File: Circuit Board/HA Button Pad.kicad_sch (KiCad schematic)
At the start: 59 parts, among them J1 Barrel_Jack, P1 USB C Connector, Q1 PN2222A, SW1 Button 1, SW2 Button 2, SW3 Button 3, SW4 Button 4, SW5 Bank Up, SW6 Bank Down, SW7 Program Button, U1 WT32-ETH01, U3 CP2102N, U4 Char LCD I2C, U5 Button I2C

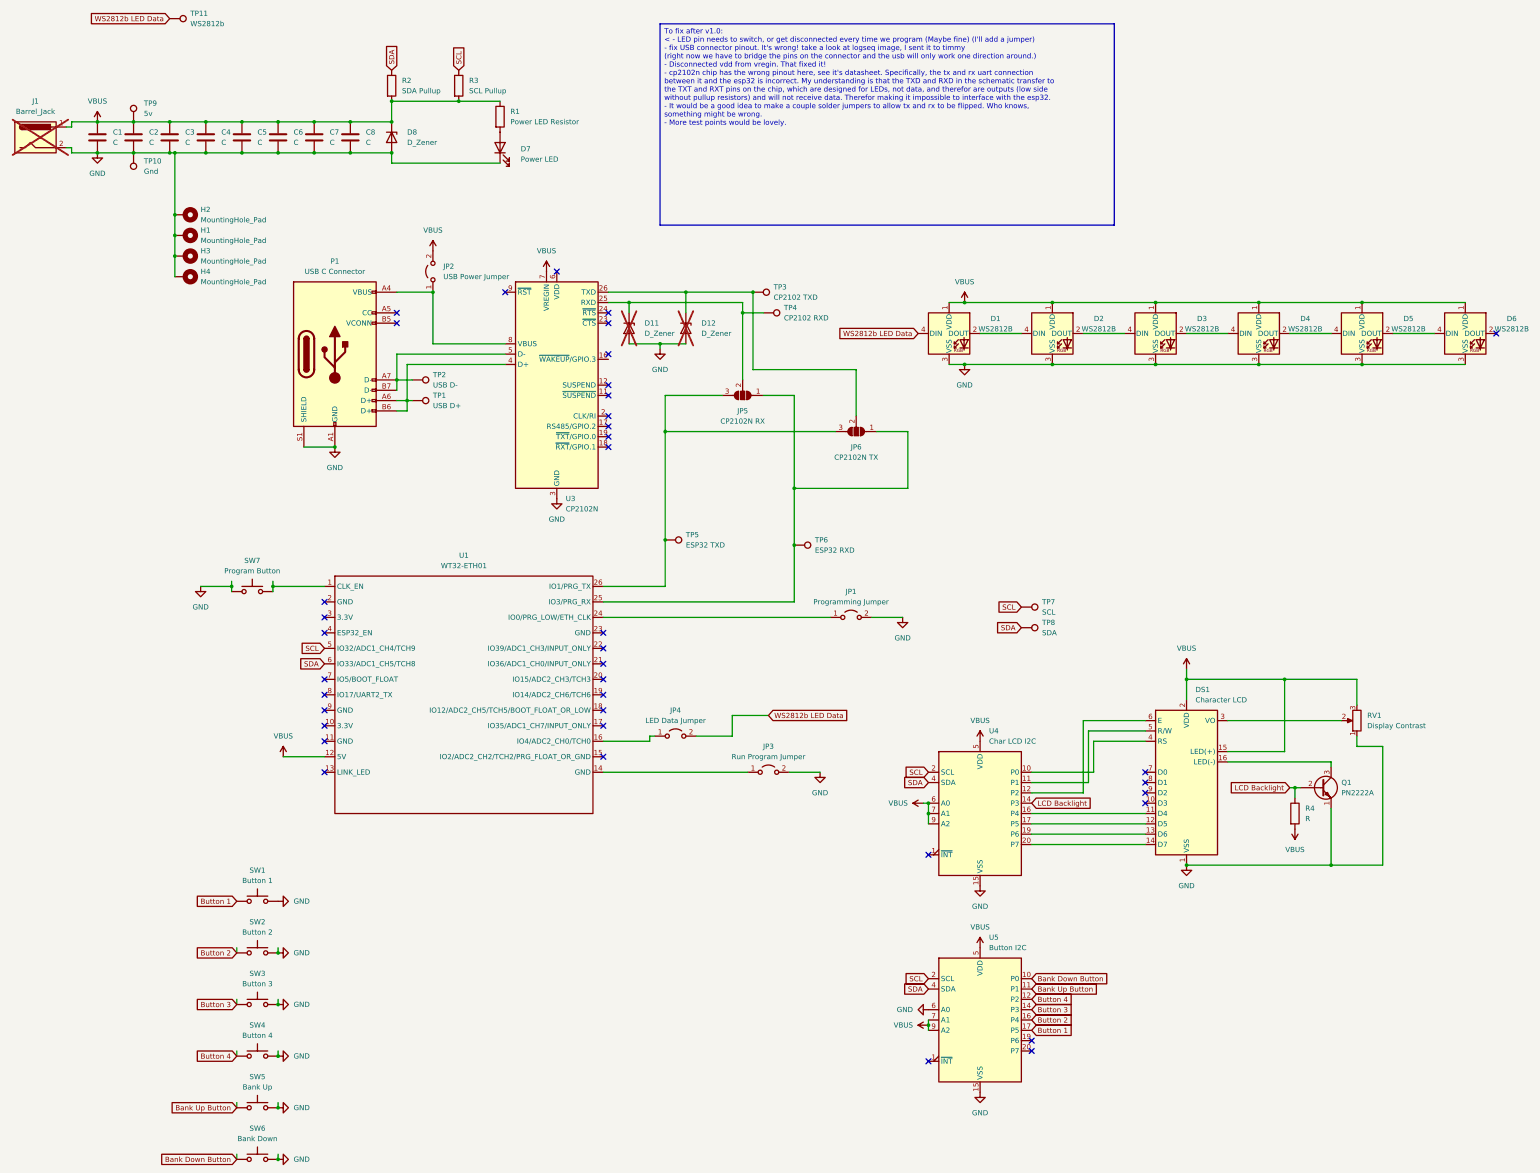
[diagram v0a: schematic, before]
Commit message: Added Capacitive Touch, changed ESP32 Pin Assignment
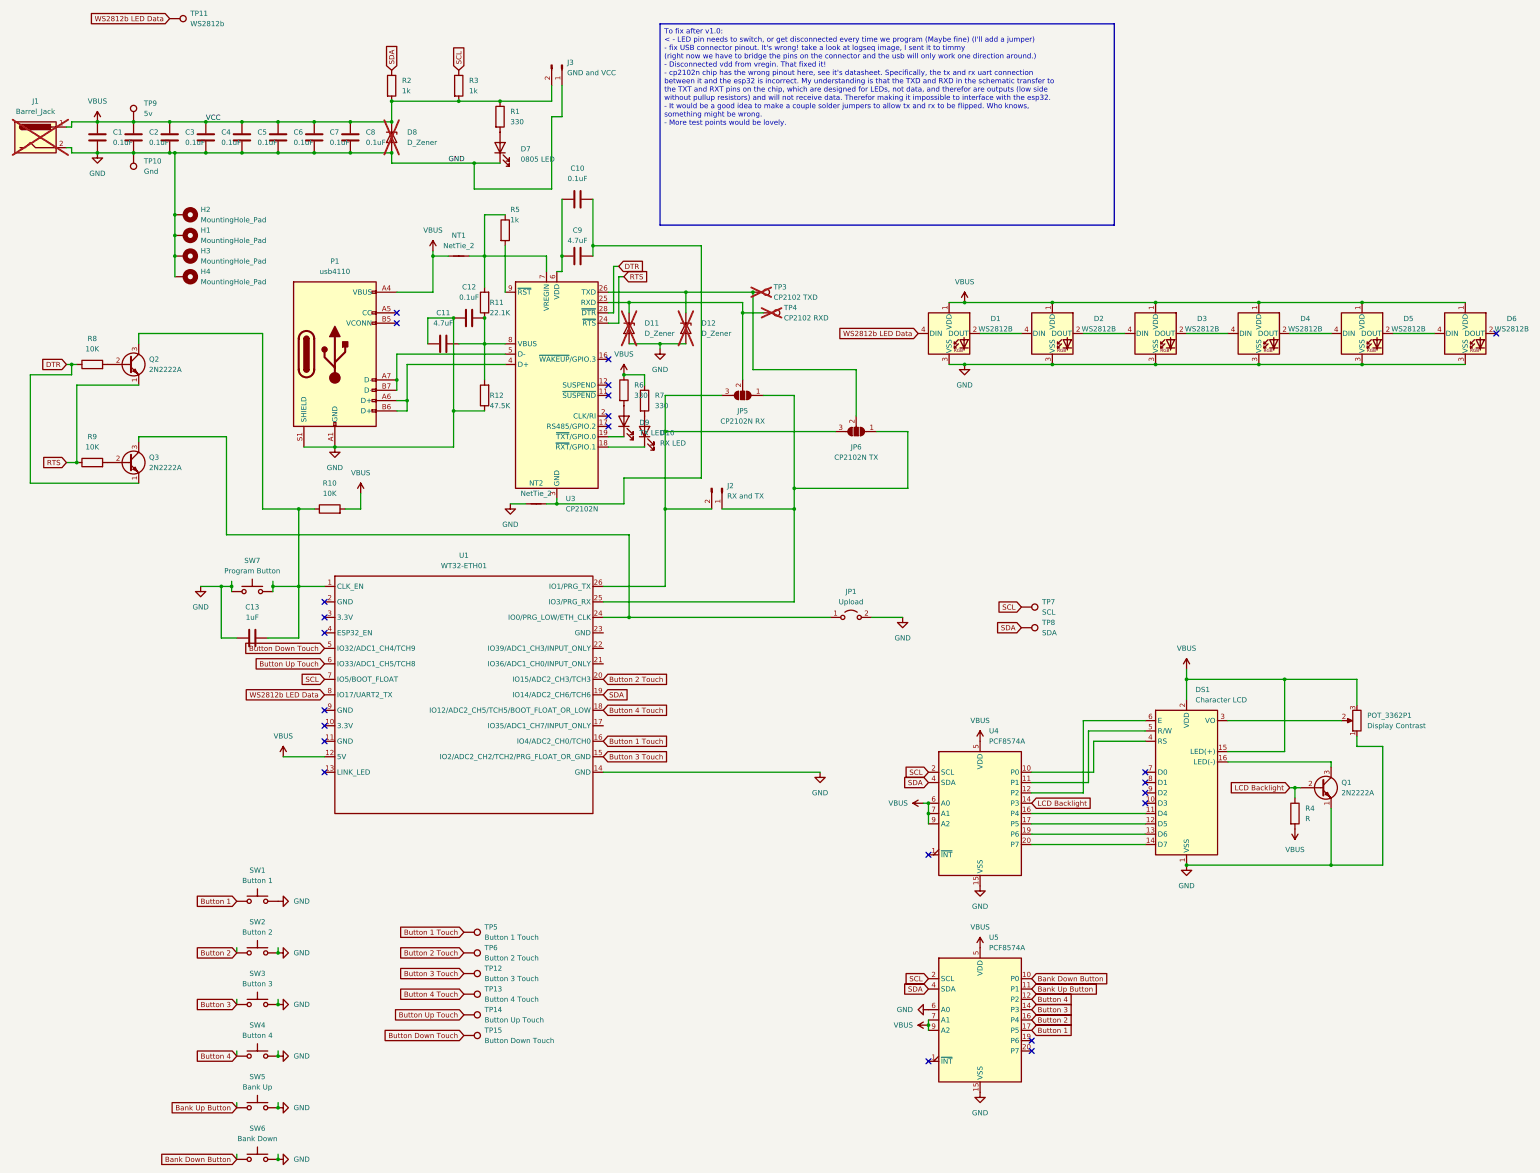
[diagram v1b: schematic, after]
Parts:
- removed JP2: USB Power Jumper, Connector_PinHeader_2.54mm:PinHeader_1x02_P2.54mm_Vertical, symbol Jumper:Jumper_2_Open
- removed JP3: Run Program Jumper, Connector_PinHeader_2.54mm:PinHeader_1x02_P2.54mm_Vertical, symbol Jumper:Jumper_2_Open
- removed JP4: LED Data Jumper, Connector_PinHeader_2.54mm:PinHeader_1x02_P2.54mm_Vertical, symbol Jumper:Jumper_2_Open
- removed TP1: USB D+, TestPoint:TestPoint_Pad_D1.0mm, symbol Connector:TestPoint
- removed TP2: USB D-, TestPoint:TestPoint_Pad_D1.0mm, symbol Connector:TestPoint
- added C10, C12: 0.1uF, capacitor model:CAPC340180_88N_KEM, symbol Device:C
- added C11, C9: 4.7uF, capacitor model:CAPC340180_88N_KEM, symbol Device:C
- added C13: 1uF, capacitor model:CAPC340180_88N_KEM, symbol Device:C
- added D10: RX LED, LED_SMD:LED_0805_2012Metric, symbol Device:LED
- added D9: TX LED, LED_SMD:LED_0805_2012Metric, symbol Device:LED
- added J2: RX and TX, Connector_PinHeader_2.54mm:PinHeader_1x02_P2.54mm_Vertical, symbol Connector:Conn_01x02_Pin
- added J3: GND and VCC, Connector_PinHeader_2.54mm:PinHeader_1x02_P2.54mm_Vertical, symbol Connector:Conn_01x02_Pin
- added NT1, NT2: NetTie_2, NetTie:NetTie-2_SMD_Pad0.5mm, symbol Device:NetTie_2
- added Q2, Q3: 2N2222A, Package_TO_SOT_THT:TO-92_Inline, symbol Transistor_BJT:PN2222A
- added R10, R8, R9: 10K, Resistor_SMD:R_0805_2012Metric, symbol Device:R
- added R11: 22.1K, Resistor_SMD:R_0805_2012Metric, symbol Device:R
- added R12: 47.5K, Resistor_SMD:R_0805_2012Metric, symbol Device:R
- added R5: 1k, Resistor_SMD:R_0805_2012Metric, symbol Device:R
- added R6, R7: 330, Resistor_SMD:R_0805_2012Metric, symbol Device:R
- added TP12: Button 3 Touch, TestPoint:TestPoint_THTPad_2.5x2.5mm_Drill1.2mm, symbol Connector:TestPoint
- added TP13: Button 4 Touch, TestPoint:TestPoint_THTPad_2.5x2.5mm_Drill1.2mm, symbol Connector:TestPoint
- added TP14: Button Up Touch, TestPoint:TestPoint_THTPad_2.5x2.5mm_Drill1.2mm, symbol Connector:TestPoint
- added TP15: Button Down Touch, TestPoint:TestPoint_THTPad_2.5x2.5mm_Drill1.2mm, symbol Connector:TestPoint
- C1, C2, C3, C4, C5, C6, C7, C8: value C -> 0.1uF
- D7: value Power LED -> 0805 LED; footprint LED_SMD:LED_0603_1608Metric -> LED_SMD:LED_0805_2012Metric
- D8, TP3, TP4: now not fitted; now left out of the parts list
- DS1, SW1, SW2, SW3, SW4, SW5, SW6, U1: now left out of the parts list
- JP1: value Programming Jumper -> Upload
- P1: value USB C Connector -> usb4110
- Q1: value PN2222A -> 2N2222A
- R1: value Power LED Resistor -> 330; footprint Resistor_SMD:R_0603_1608Metric -> Resistor_SMD:R_0805_2012Metric
- R2: value SDA Pullup -> 1k; footprint Resistor_SMD:R_0603_1608Metric -> Resistor_SMD:R_0805_2012Metric
- R3: value SCL Pullup -> 1k; footprint Resistor_SMD:R_0603_1608Metric -> Resistor_SMD:R_0805_2012Metric
- R4: footprint Resistor_SMD:R_0603_1608Metric -> Resistor_SMD:R_0805_2012Metric
- TP5: value ESP32 TXD -> Button 1 Touch; footprint TestPoint:TestPoint_Pad_D1.0mm -> TestPoint:TestPoint_THTPad_2.5x2.5mm_Drill1.2mm
- TP6: value ESP32 RXD -> Button 2 Touch; footprint TestPoint:TestPoint_Pad_D1.0mm -> TestPoint:TestPoint_THTPad_2.5x2.5mm_Drill1.2mm
- U4: value Char LCD I2C -> PCF8574A
- U5: value Button I2C -> PCF8574A
- renumbered RV1 to POT_3362P1
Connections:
- net GND: now also U1.14 (GND), C11.1, C12.1, C13.1, J3.1 (Pin_1), NT2.1, R12.1; no longer U3.12 (SUSPEND), U3.21 (GND), U3.3 (GND)
- net SCL: now also U1.7 (IO5/BOOT_FLOAT); no longer U1.5 (IO32/ADC1_CH4/TCH9)
- net SDA: now also U1.19 (IO14/ADC2_CH6/TCH6); no longer U1.6 (IO33/ADC1_CH5/TCH8)
- net VBUS: now also P1.A4 (VBUS), P1.A9 (VBUS), P1.B4 (VBUS), P1.B9 (VBUS), J3.2 (Pin_2), NT1.1, R10.2, R6.1, R7.1; no longer U3.7 (VREGIN)
- net WS2812b LED Data: now also U1.8 (IO17/UART2_TX)
- net at JP5.1 (A), JP6.1 (A), U1.25 (IO3/PRG_RX): now also J2.1 (Pin_1); no longer TP6.1
- net at JP5.3 (B), JP6.3 (B), U1.26 (IO1/PRG_TX): now also J2.2 (Pin_2); no longer TP5.1
- net at SW7.2, U1.1 (CLK_EN): now also C13.2, Q2.3 (C), R10.1
- net Button 3 Touch: now reaches U1.15 (IO2/ADC2_CH2/TCH2/PRG_FLOAT_OR_GND)
- net Button 3 Touch: now also TP12.1
- net Button 1 Touch: now reaches U1.16 (IO4/ADC2_CH0/TCH0)
- net Button 1 Touch: now also TP5.1
- net Button 4 Touch: now reaches U1.18 (IO12/ADC2_CH5/TCH5/BOOT_FLOAT_OR_LOW)
- net Button 4 Touch: now also TP13.1
- net Button 2 Touch: now reaches U1.20 (IO15/ADC2_CH3/TCH3)
- net Button 2 Touch: now also TP6.1
- net at JP1.1 (A), U1.24 (IO0/PRG_LOW/ETH_CLK): now also Q3.3 (C)
- net at U3.18 (~{RXT}/GPIO.1): now also D10.1 (K)
- net at U3.19 (~{TXT}/GPIO.0): now also D9.1 (K)
- net RTS: now reaches U3.24 (~{RTS})
- net RTS: now also Q2.1 (E), R9.1
- net at U3.6 (VDD): now also C10.1, C9.1
- net at U3.9 (~{RST}): now also R5.2
- new net: D9.2 (A), R6.2
- new net: C10.2, C9.2, NT2.2, U3.12 (SUSPEND), U3.21 (GND), U3.3 (GND)
- new net: C11.2, C12.2, R11.1, R12.2, U3.8 (VBUS)
- new net: NT1.2, R11.2, R5.1, U3.7 (VREGIN)
- new net: Q3.2 (B), R9.2
- new net: D10.2 (A), R7.2
- new net: Q2.2 (B), R8.2
- new net Button Down Touch: TP15.1, U1.5 (IO32/ADC1_CH4/TCH9)
- new net Button Up Touch: TP14.1, U1.6 (IO33/ADC1_CH5/TCH8)
- new net DTR: Q3.1 (E), R8.1, U3.28 (~{DTR})
- no-connect marks 39 -> 23
